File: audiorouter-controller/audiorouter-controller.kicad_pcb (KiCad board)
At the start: 2 copper layers, 86.4 x 45.7 mm, 11 parts, among them J1 ToBoards, J2 PowerIn

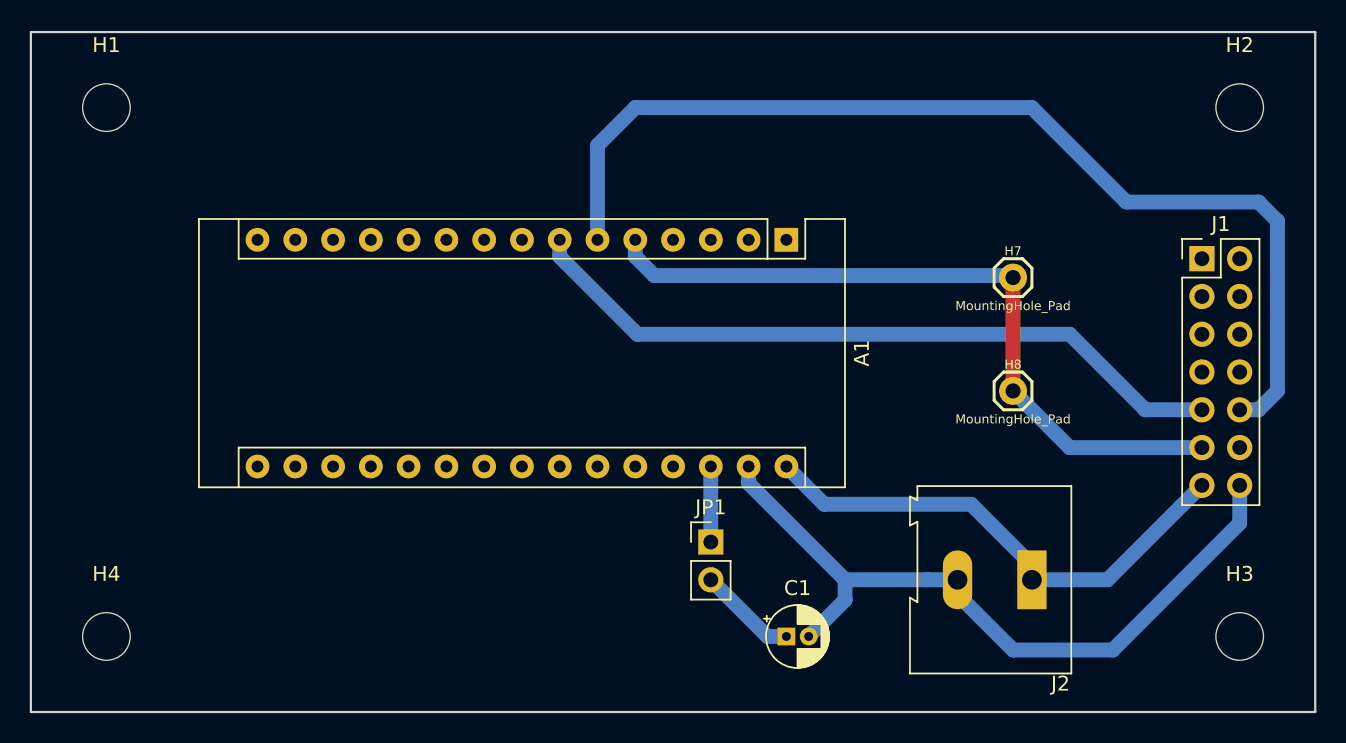
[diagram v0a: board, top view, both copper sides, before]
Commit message: Turned out that time delay circut for 595 output enable pins was bad idea in practice. I reworked my device by removing timed pull-down circuit components while leaving pull-up in place. Added wires to 12. pin both incoming and outgoing ribbon cables for pull-down from controller board. Added pulldown wire to controller.
Rewrote controller board arduino software for output enable logic.
Fixed bugs that caused parasitic powering of daughter boards via
595 data pins. Worked around noise induced false triggering by
overwriting correct state to 595 cascade every second. Added
software logic for drawn current limiting.
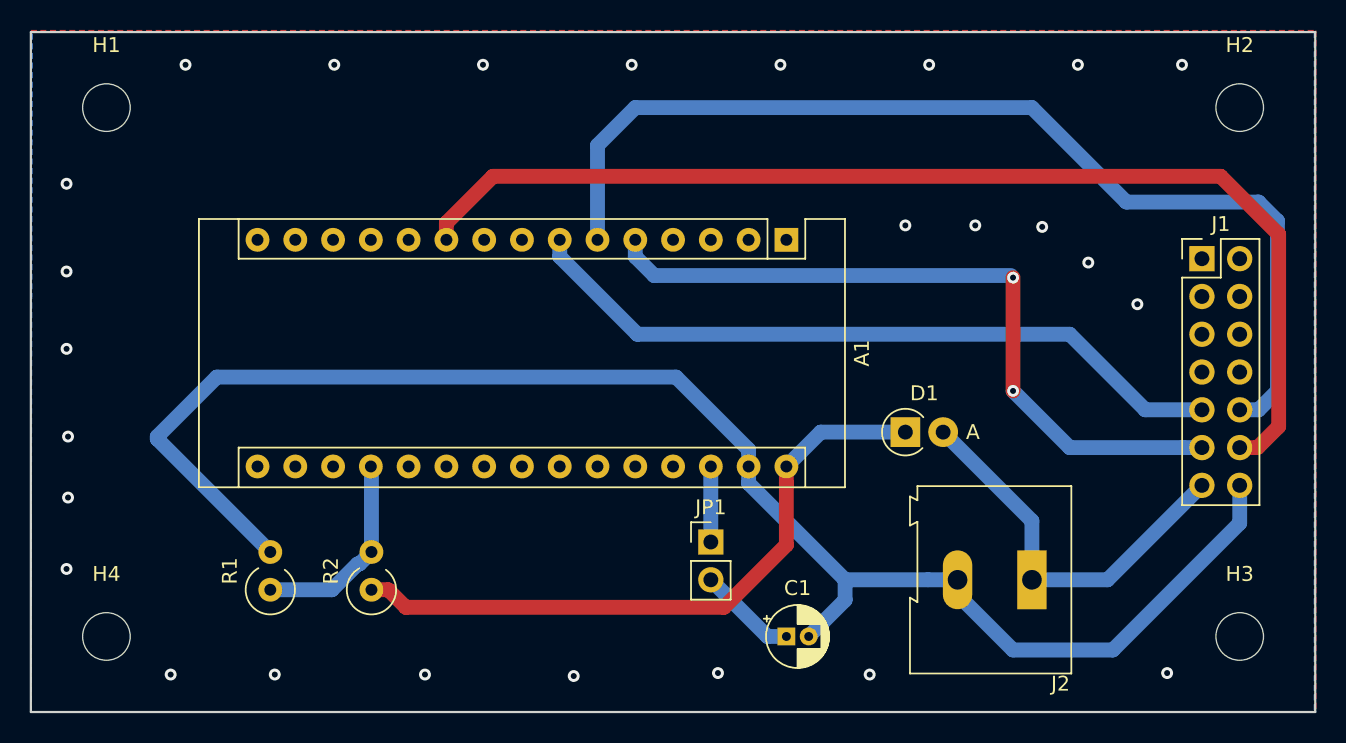
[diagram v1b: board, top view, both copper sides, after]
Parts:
- removed H7, H8: MountingHole_Pad, Connectors:1X01
- added D1: N4007, Diode_THT:D_T-1_P2.54mm_Vertical_AnodeUp, F.Cu at (160.4, 77.7)
- added R1: 6.8k, Resistor_THT:R_Axial_DIN0309_L9.0mm_D3.2mm_P2.54mm_Vertical, F.Cu at (117.7, 88.3)
- added R2: 6.8k, Resistor_THT:R_Axial_DIN0309_L9.0mm_D3.2mm_P2.54mm_Vertical, F.Cu at (124.5, 88.3)
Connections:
- A1 pad 10: (no net) -> OutputEnable
- A1 pad 19: (no net) -> PowerMeasure
- A1 pad 30: PowerIn -> Net-(A1-Pad30)
- J1 pad 12: (no net) -> OutputEnable
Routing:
- net OutputEnable: track 0.00 -> 76.1 mm
- net GND: track 50.2 -> 105.7 mm, vias 0 -> 26
- net Net-(A1-Pad30): track 0.00 -> 44.4 mm
- net PowerMeasure: track 0.00 -> 13.6 mm
- net PowerIn: track 34.3 -> 27.5 mm
- added copper zone on B.Cu, net GND
- added copper zone on F.Cu, net GND

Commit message: Next revison: hardware support for lcd character display and matrix keyboards. Should be generic enough to connect something else when ideas changes. Last revision was for home-made pcb. This revision has too narrow clearences for that.
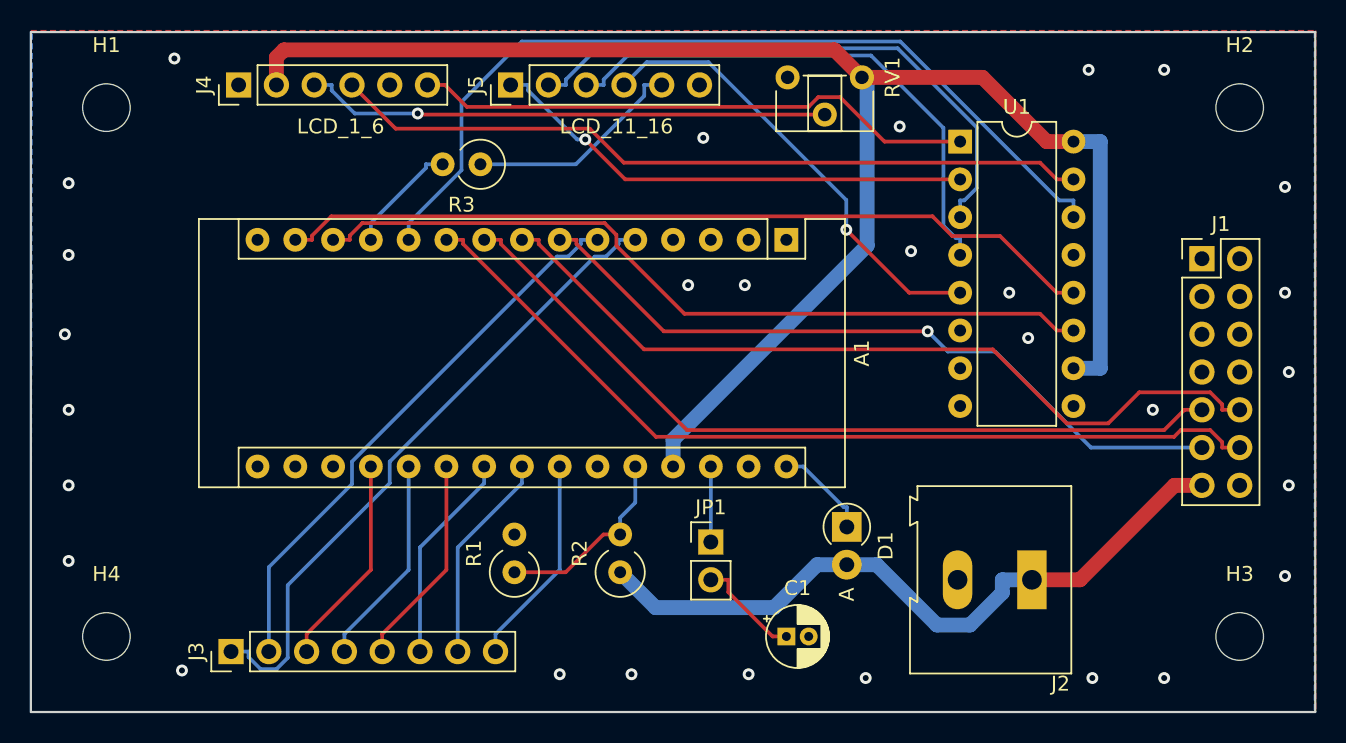
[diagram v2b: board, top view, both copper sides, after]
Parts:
- added J3: AUX, Connector_PinHeader_2.54mm:PinHeader_1x08_P2.54mm_Vertical, F.Cu at (115.1, 92.5)
- added J4: LCD_1_6, Connector_PinHeader_2.54mm:PinHeader_1x06_P2.54mm_Vertical, F.Cu at (115.6, 54.4)
- added J5: LCD_11_16, Connector_PinHeader_2.54mm:PinHeader_1x06_P2.54mm_Vertical, F.Cu at (133.9, 54.4)
- added R3: 220, Resistor_THT:R_Axial_DIN0309_L9.0mm_D3.2mm_P2.54mm_Vertical, F.Cu at (131.8, 59.7)
- added RV1: 10k, Potentiometer_THT:Potentiometer_ACP_CA6-H2,5_Horizontal, F.Cu at (157.5, 53.8)
- added U1: 74HC595, Package_DIP:DIP-16_W7.62mm, F.Cu at (164.1, 58.2)
- R1: value 6.8k -> 33k
- R2: value 6.8k -> 47k
- moved R2 16.8 mm to (141.2, 87.1)
- moved R1 16.5 mm to (134.1, 87.1)
- moved D1 7.49 mm to (156.5, 84.1), turned to 270 degrees
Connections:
- A1 pad 11: (no net) -> LCD_SerialOut
- A1 pad 12: (no net) -> LCD_LED
- A1 pad 13: (no net) -> LCD_SerialClock
- A1 pad 14: (no net) -> LCD_RClock
- A1 pad 19: PowerMeasure -> AUX3
- A1 pad 20: (no net) -> AUX4
- A1 pad 21: (no net) -> AUX5
- A1 pad 22: (no net) -> AUX6
- A1 pad 23: (no net) -> AUX7
- A1 pad 24: (no net) -> AUX8
- A1 pad 26: (no net) -> PowerMeasure
- A1 pad 27: (no net) -> +5V
- A1 pad 5: SerialClock -> AUX1
- A1 pad 6: RClock -> AUX2
- A1 pad 7: SerialOut -> SerialClock
- A1 pad 8: (no net) -> RClock
- A1 pad 9: (no net) -> SerialOut
- R2 pad 1: Net-(A1-Pad30) -> PowerIn
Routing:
- net +5V: track 0.00 -> 108.8 mm
- net GND: track 105.7 -> 0.00 mm, vias 26 -> 29
- net LCD_SerialOut: track 0.00 -> 59.1 mm
- net LCD_RClock: track 0.00 -> 55.3 mm
- net LCD_SerialClock: track 0.00 -> 53.8 mm
- net Net-(J4-Pad4): track 0.00 -> 51.1 mm
- net AUX1: track 0.00 -> 43.7 mm
- net Net-(J5-Pad2): track 0.00 -> 38.9 mm
- net AUX2: track 0.00 -> 37.9 mm
- net Net-(J4-Pad6): track 0.00 -> 37.9 mm
- net Net-(A1-Pad30): track 44.4 -> 6.52 mm
- net Net-(J5-Pad3): track 0.00 -> 36.2 mm
- net Net-(J4-Pad3): track 0.00 -> 35.4 mm, vias 0 -> 1
- net Net-(J5-Pad1): track 0.00 -> 33.1 mm, vias 0 -> 1
- net Net-(J5-Pad4): track 0.00 -> 30.8 mm, vias 0 -> 1
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
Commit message: Bummer, some of the ground plane was left unconnected. I bodged with wire and won't order new pcbs. Fixing in repo regardless.
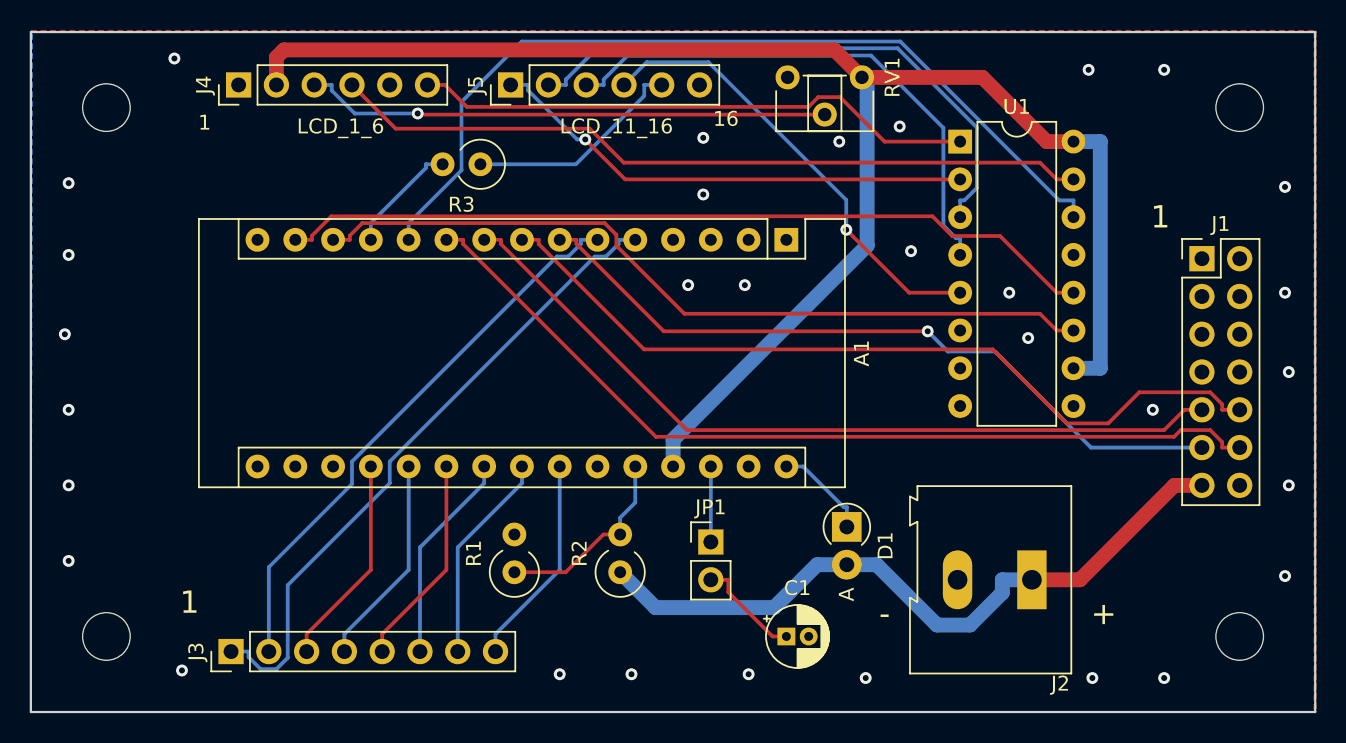
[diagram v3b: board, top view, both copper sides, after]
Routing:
- net GND: vias 29 -> 31
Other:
- board text added: "+"
- board text added: "-"
- board text added: "1"
- board text added: "16"
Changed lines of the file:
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@@
-(kicad_pcb (version 20171130) (host pcbnew 5.1.5-1.fc31)
+(kicad_pcb (version 20171130) (host pcbnew 5.1.5-2.fc32)
   (general
     (thickness 1.6)
-    (drawings 4)
-    (tracks 231)
+    (drawings 10)
+    (tracks 233)
     (zones 0)
     (modules 18)
@@
     (tags "mounting hole 3.2mm no annular m3")
     (attr virtual)
-    (fp_text reference H1 (at 0 -4.2) (layer F.SilkS)
+    (fp_text reference H1 (at 0 -4.2) (layer F.SilkS) hide
       (effects (font (size 1 1) (thickness 0.15)))
     )
@@
     (tags "mounting hole 3.2mm no annular m3")
     (attr virtual)
-    (fp_text reference H2 (at 0 -4.2) (layer F.SilkS)
+    (fp_text reference H2 (at 0 -4.2) (layer F.SilkS) hide
       (effects (font (size 1 1) (thickness 0.15)))
     )
@@
     (tags "mounting hole 3.2mm no annular m3")
     (attr virtual)
-    (fp_text reference H3 (at 0 -4.2) (layer F.SilkS)
+    (fp_text reference H3 (at 0 -4.2) (layer F.SilkS) hide
       (effects (font (size 1 1) (thickness 0.15)))
     )
@@
     (tags "mounting hole 3.2mm no annular m3")
     (attr virtual)
-    (fp_text reference H4 (at 0 -4.2) (layer F.SilkS)
+    (fp_text reference H4 (at 0 -4.2) (layer F.SilkS) hide
       (effects (font (size 1 1) (thickness 0.15)))
     )
@@
     )
   )
+  (gr_text 16 (at 148.336 56.642) (layer F.SilkS)
+    (effects (font (size 1 1) (thickness 0.15)))
+  )
+  (gr_text 1 (at 113.284 56.896) (layer F.SilkS)
+    (effects (font (size 1 1) (thickness 0.15)))
+  )
+  (gr_text 1 (at 112.268 89.154) (layer F.SilkS)
+    (effects (font (size 1.5 1.5) (thickness 0.3)))
+  )
+  (gr_text 1 (at 177.546 63.246) (layer F.SilkS)
+    (effects (font (size 1.5 1.5) (thickness 0.3)))
+  )
+  (gr_text - (at 159.004 89.916) (layer F.SilkS)
+    (effects (font (size 1.5 1.5) (thickness 0.3)))
+  )
+  (gr_text + (at 173.736 89.916) (layer F.SilkS)
+    (effects (font (size 1.5 1.5) (thickness 0.3)))
+  )
   (gr_line (start 101.6 96.52) (end 101.6 50.8) (layer Edge.Cuts) (width 0.15))
   (gr_line (start 187.96 96.52) (end 101.6 96.52) (layer Edge.Cuts) (width 0.15))
   (gr_line (start 187.96 50.8) (end 187.96 96.52) (layer Edge.Cuts) (width 0.15))
   (gr_line (start 101.6 50.8) (end 187.96 50.8) (layer Edge.Cuts) (width 0.15))
+  (via (at 146.812 61.722) (size 0.8) (drill 0.4) (layers F.Cu B.Cu) (net 5))
   (segment (start 137.16 64.77) (end 138.2853 64.77) (width 0.25) (layer F.Cu) (net 1))
   (segment (start 161.9015 70.922) (end 144.156 70.922) (width 0.25) (layer F.Cu) (net 1))
@@
   (via (at 172.72 53.34) (size 0.8) (drill 0.4) (layers F.Cu B.Cu) (net 5))
   (via (at 111.252 52.578) (size 0.8) (drill 0.4) (layers F.Cu B.Cu) (net 5))
+  (via (at 155.956 58.166) (size 0.8) (drill 0.4) (layers F.Cu B.Cu) (net 5))
   (segment (start 180.34 81.28) (end 178.4897 81.28) (width 1) (layer F.Cu) (net 6))
   (segment (start 168.91 87.63) (end 172.1397 87.63) (width 1) (layer F.Cu) (net 6))
